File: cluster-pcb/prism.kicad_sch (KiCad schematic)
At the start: 8 parts, among them J501 Conn_01x04_P3.5mm_TBH_Horizon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, U501 Interface_RS485_MAX13431E, U502 TPS1H200AQDGNRQ1

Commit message: First SPI changes
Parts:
- removed C502: 1uF_35V, Janelia:C_0402_1005Metric, symbol Janelia:C_1uF_35V_0402
- removed U501: Interface_RS485_MAX13431E, Janelia:21-0137I_T1033-1_MXM, symbol Janelia:Interface_RS485_MAX13431E
- added C502: 0.1uF_100V, Janelia:C_0402_1005Metric, symbol Janelia:C_0.1uF_100V_0402
- added C503: 27pF_50V, Janelia:C_0402_1005Metric, symbol Janelia:C_27pF_50V_0402
- added FL501: Choke_CMF_ACT45B-220-2P, Janelia:SMD_0-2P-TL003_TDK-L, symbol Janelia:Choke_CMF_ACT45B-220-2P
- added R503: 1.4k, Janelia:R_0402_1005Metric, symbol Janelia:R_1.4k_0402
- added R504: 604, Janelia:R_0402_1005Metric, symbol Janelia:R_604_0402
- added TR501: 1:1, Janelia:FB020G00, symbol Janelia:Transformer_Pulse_1CT{colon}1CT_SMD
- added U501: LTC6820HMS-TRPBF, Janelia:MS_05-08-1669_ADI, symbol Janelia:LTC6820HMS-TRPBF
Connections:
- net +3.3V: no longer C501.1
- net +5V: now also C501.1, C502.1, U501.1 (EN), U501.6 (VDDS), U501.7 (POL), U501.8 (PHA), U501.9 (VDD)
- net GND: now also C502.2, C503.2, R504.2, U501.12 (MSTR), U501.13 (SLOW), U501.14 (GND)
- net SWN renamed IM
- net IM: now also TR501.4 (MX-); no longer R501.2
- net SWP renamed IP
- net IP: now also TR501.5 (MX+); no longer R501.1
- new net CIPO: U501.3 (MISO)
- new net COPI: U501.2 (MOSI)
- new net CT: C503.1, TR501.6 (TCT)
- new net IBIAS: R503.1, U501.16 (IBIAS)
- new net ICMP: R503.2, R504.1, U501.15 (ICMP)
- new net IM1: FL501.3, TR501.2 (TD-)
- new net IM2: FL501.2, R501.2, U501.10 (IM)
- new net IP1: FL501.4, TR501.1 (TD+)
- new net IP2: FL501.1, R501.1, U501.11 (IP)
- new net SCK: U501.4 (SCK)
- new net ~{CS}: U501.5 (~{CS})
- no-connect marks 1 -> 2
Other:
- note added: "FAST MODE"
- note added: "NO IDLE"
- note added: "RB1"
- note added: "RB2"
- note added: "SPI MODE 3"
- moved on the sheet: D501, R502, U502

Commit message: Progress toward v2.0
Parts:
- removed J501: Conn_01x04_P3.5mm_TBH_Horizontal_Screw, Janelia:PhoenixContact_MC_1,5_4-G-3.5_1x04_P3.50mm_Horizontal_Screw, symbol Janelia:Conn_01x04_P3.5mm_TBH_Horizontal_Screw
- removed R501: 120, Janelia:R_0402_1005Metric, symbol Janelia:R_120_0402
- added J501: USB_C_Receptacle_USB2.0_16P_GT-USB-7047C, Janelia:USB_C_Receptacle_GT-USB-7047C_16P_TopMnt_Horizontal, symbol Janelia:USB_C_Receptacle_USB2.0_16P_GT-USB-7047C
- added R501: 100, Janelia:R_0402_1005Metric, symbol Janelia:R_100_0402
- added R505: 100k, Janelia:R_0402_1005Metric, symbol Janelia:R_100k_0402
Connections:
- net +3.3V: now also C501.1, U501.6 (VDDS), R505.1
- net +5V: no longer C501.1, U501.6 (VDDS)
- net CIPO: now also R505.2
- net GND: now also J501.A1 (GND), J501.A12 (GND), J501.B1 (GND), J501.B12 (GND), J501.S1 (SHIELD)
- net VCC: now also J501.A4 (VBUS), J501.A9 (VBUS), J501.B4 (VBUS), J501.B9 (VBUS)
- net IM renamed I0-
- net I0-: now also J501.A7 (D-), J501.B7 (D-)
- net IM1 renamed I1-
- net IM2 renamed I2-
- net I2-: now also R501.2
- net IP renamed I0+
- net I0+: now also J501.A6 (D+), J501.B6 (D+)
- net IP1 renamed I1+
- net IP2 renamed I2+
- net I2+: now also R501.1
- no-connect marks 2 -> 6
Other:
- note added: "USB C Cable Differential Impedance 90 Ohm"
- moved on the sheet: D501, R502, U502

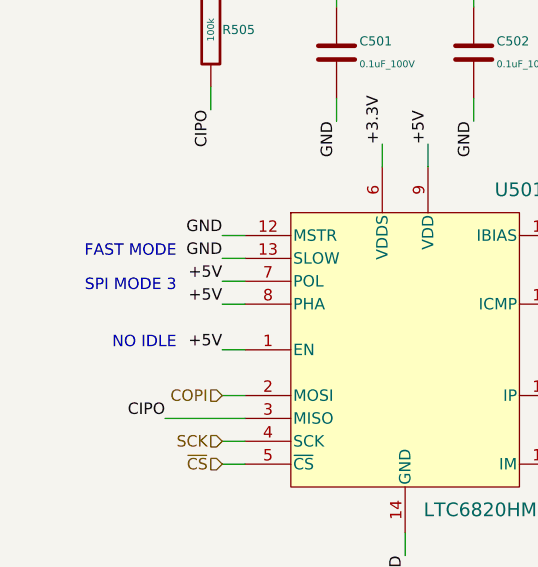
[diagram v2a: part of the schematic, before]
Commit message: Initial pcb layout
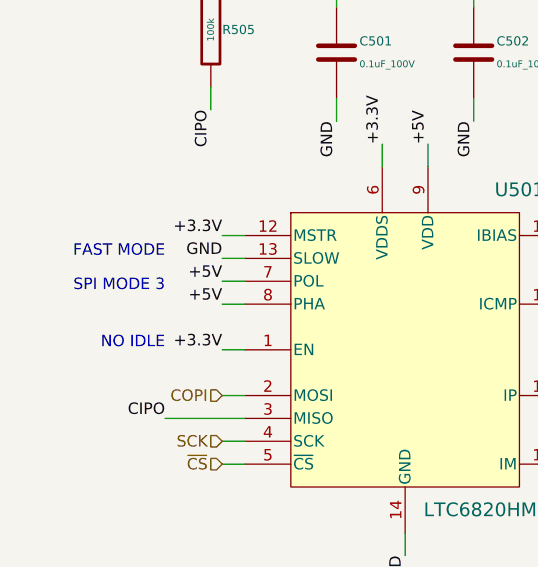
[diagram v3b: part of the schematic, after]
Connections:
- net +3.3V: now also U501.1 (EN), U501.12 (MSTR)
- net +5V: no longer U501.1 (EN)
- net GND: no longer U501.12 (MSTR)
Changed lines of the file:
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@@
   (title_block
     (title "cluster-pcb")
-    (date "2024-09-20")
+    (date "2024-09-27")
     (rev "2.0")
     (company "Howard Hughes Medical Institute")
@@
     (effects (font (size 1.27 1.27)) (justify right bottom))
   )
-  (text "NO IDLE" (at 52.07 134.62 0)
+  (text "NO IDLE" (at 50.8 134.62 0)
     (effects (font (size 1.27 1.27)) (justify right bottom))
   )
@@
     (effects (font (size 1.27 1.27)) (justify right bottom))
   )
-  (text "SPI MODE 3" (at 52.07 128.27 0)
-    (effects (font (size 1.27 1.27)) (justify right bottom))
-  )
-  (text "FAST MODE" (at 52.07 124.46 0)
+  (text "SPI MODE 3" (at 50.8 128.27 0)
+    (effects (font (size 1.27 1.27)) (justify right bottom))
+  )
+  (text "FAST MODE" (at 50.8 124.46 0)
     (effects (font (size 1.27 1.27)) (justify right bottom))
   )
@@
     (effects (font (size 1.27 1.27)) (justify right bottom))
   )
+  (label "+3.3V" (at 57.15 134.62 180) (fields_autoplaced)
+    (effects (font (size 1.27 1.27)) (justify right bottom))
+  )
   (label "I2+" (at 106.68 134.62 90) (fields_autoplaced)
     (effects (font (size 1.27 1.27)) (justify left bottom))
@@
     (effects (font (size 1.27 1.27)) (justify right bottom))
   )
-  (label "GND" (at 57.15 121.92 180) (fields_autoplaced)
-    (effects (font (size 1.27 1.27)) (justify right bottom))
-  )
   (label "GND" (at 139.7 149.86 270) (fields_autoplaced)
     (effects (font (size 1.27 1.27)) (justify right bottom))
   )
+  (label "+3.3V" (at 57.15 121.92 180) (fields_autoplaced)
+    (effects (font (size 1.27 1.27)) (justify right bottom))
+  )
   (label "I0-" (at 176.53 148.59 0) (fields_autoplaced)
     (effects (font (size 1.27 1.27)) (justify left bottom))
@@
     (effects (font (size 1.27 1.27)) (justify right bottom))
   )
-  (label "+5V" (at 57.15 134.62 180) (fields_autoplaced)
-    (effects (font (size 1.27 1.27)) (justify right bottom))
-  )
